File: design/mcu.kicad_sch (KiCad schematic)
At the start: 35 parts, among them J2 SWD_01X04, J3 DEBUG_SPI, U6 STM32H750VBTx, X1 ASTX-H11-25.000MHZ-T, X2 SIT8209AI-21-33S-100.000000X

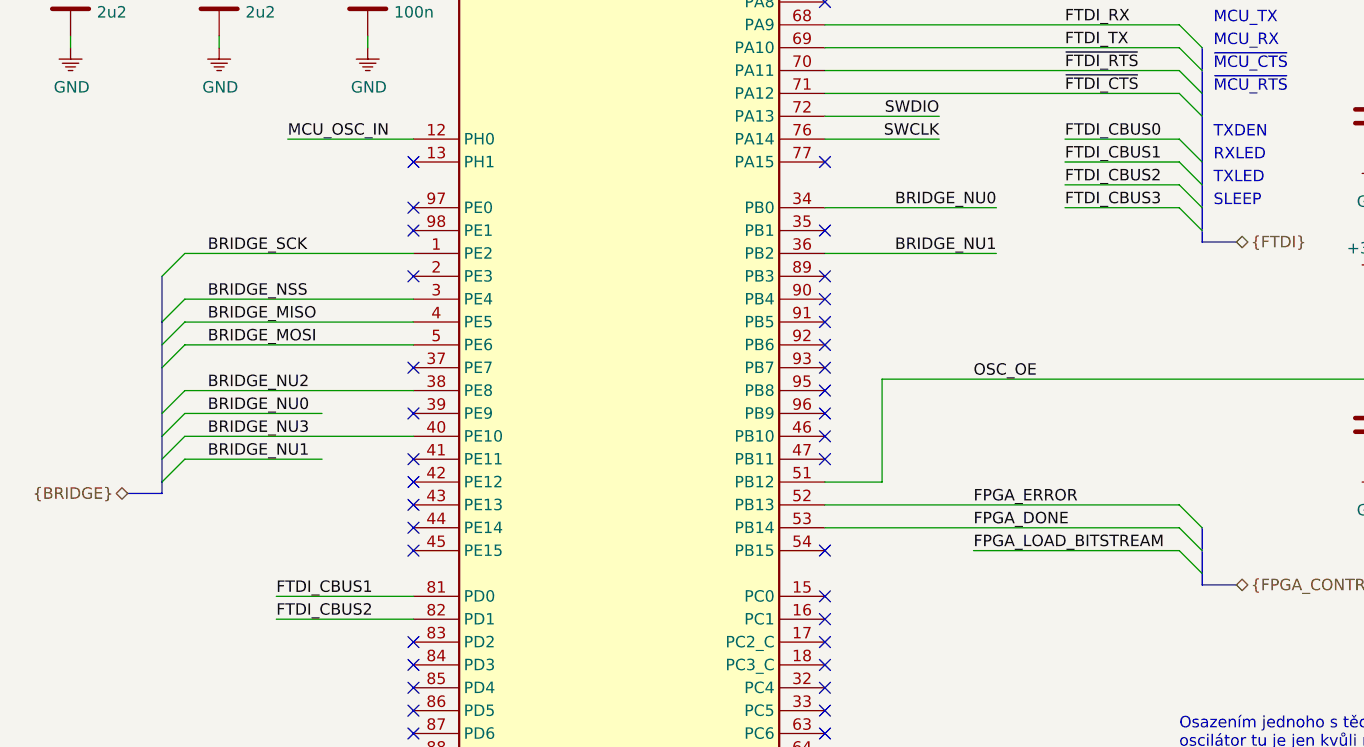
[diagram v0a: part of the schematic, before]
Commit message: Named button reset net
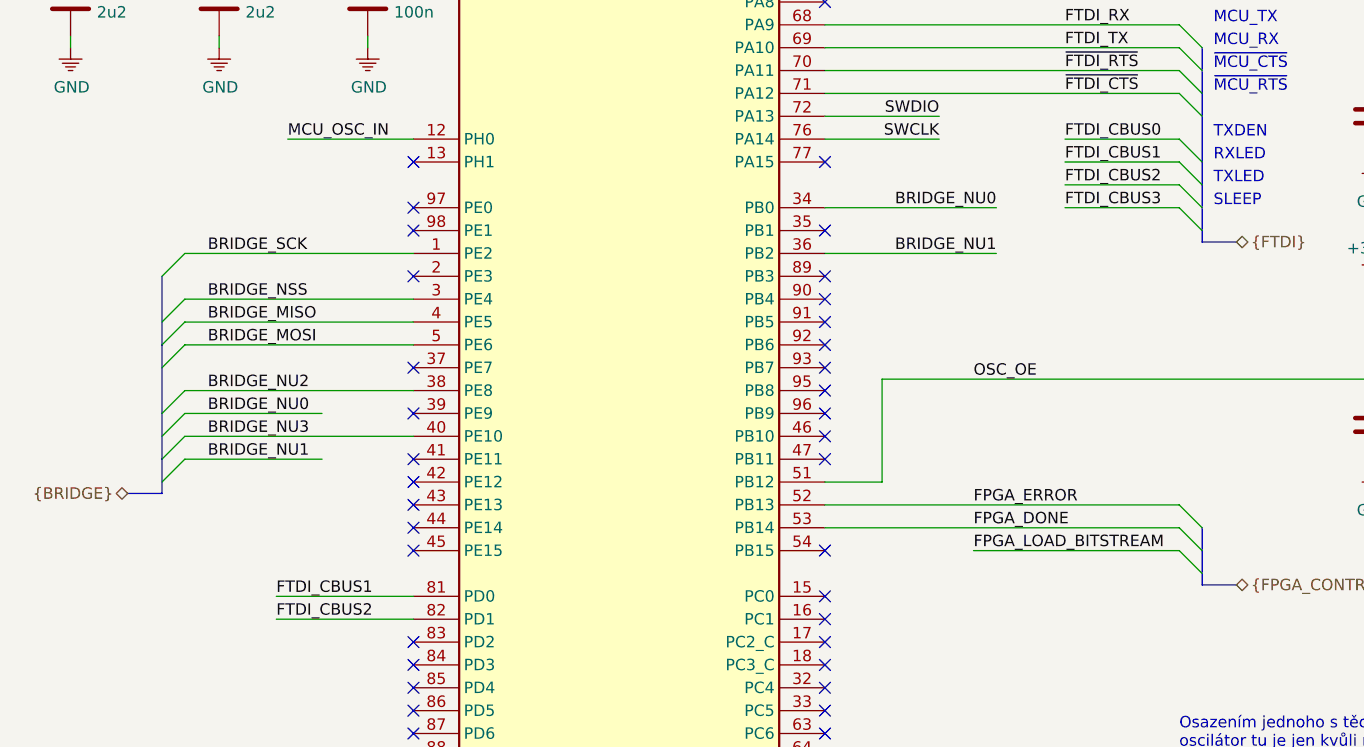
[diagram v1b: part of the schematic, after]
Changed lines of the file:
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@@
   (junction (at 236.22 25.4))
   (junction (at 262.89 26.67))
-  (no_connect (at 140.97 91.44))
+  (no_connect (at 140.97 45.72))
+  (no_connect (at 140.97 129.54))
+  (no_connect (at 95.25 109.22))
+  (no_connect (at 140.97 93.98))
+  (no_connect (at 95.25 132.08))
+  (no_connect (at 95.25 104.14))
   (no_connect (at 140.97 48.26))
-  (no_connect (at 95.25 99.06))
-  (no_connect (at 95.25 144.78))
-  (no_connect (at 140.97 43.18))
-  (no_connect (at 95.25 152.4))
-  (no_connect (at 140.97 83.82))
-  (no_connect (at 95.25 132.08))
-  (no_connect (at 140.97 40.64))
-  (no_connect (at 95.25 114.3))
-  (no_connect (at 95.25 116.84))
-  (no_connect (at 140.97 76.2))
-  (no_connect (at 140.97 129.54))
-  (no_connect (at 95.25 88.9))
-  (no_connect (at 140.97 45.72))
-  (no_connect (at 95.25 137.16))
-  (no_connect (at 140.97 96.52))
-  (no_connect (at 95.25 129.54))
-  (no_connect (at 95.25 149.86))
-  (no_connect (at 95.25 142.24))
-  (no_connect (at 140.97 134.62))
-  (no_connect (at 140.97 58.42))
-  (no_connect (at 95.25 76.2))
-  (no_connect (at 95.25 134.62))
-  (no_connect (at 140.97 144.78))
-  (no_connect (at 95.25 81.28))
+  (no_connect (at 140.97 53.34))
+  (no_connect (at 140.97 142.24))
+  (no_connect (at 95.25 139.7))
+  (no_connect (at 140.97 139.7))
+  (no_connect (at 140.97 157.48))
+  (no_connect (at 140.97 106.68))
   (no_connect (at 140.97 127))
-  (no_connect (at 95.25 139.7))
-  (no_connect (at 140.97 104.14))
-  (no_connect (at 140.97 162.56))
-  (no_connect (at 140.97 124.46))
-  (no_connect (at 95.25 83.82))
-  (no_connect (at 140.97 109.22))
+  (no_connect (at 140.97 137.16))
   (no_connect (at 140.97 38.1))
   (no_connect (at 140.97 99.06))
-  (no_connect (at 140.97 93.98))
-  (no_connect (at 140.97 137.16))
-  (no_connect (at 140.97 106.68))
-  (no_connect (at 140.97 142.24))
+  (no_connect (at 95.25 83.82))
+  (no_connect (at 95.25 88.9))
+  (no_connect (at 140.97 55.88))
+  (no_connect (at 95.25 81.28))
   (no_connect (at 140.97 50.8))
-  (no_connect (at 95.25 104.14))
+  (no_connect (at 95.25 134.62))
+  (no_connect (at 140.97 91.44))
+  (no_connect (at 140.97 96.52))
+  (no_connect (at 140.97 162.56))
+  (no_connect (at 95.25 76.2))
+  (no_connect (at 95.25 137.16))
+  (no_connect (at 95.25 129.54))
+  (no_connect (at 140.97 43.18))
+  (no_connect (at 95.25 149.86))
+  (no_connect (at 95.25 111.76))
+  (no_connect (at 140.97 76.2))
   (no_connect (at 140.97 149.86))
   (no_connect (at 140.97 119.38))
+  (no_connect (at 140.97 134.62))
+  (no_connect (at 140.97 88.9))
+  (no_connect (at 140.97 104.14))
+  (no_connect (at 95.25 144.78))
+  (no_connect (at 140.97 144.78))
+  (no_connect (at 95.25 152.4))
+  (no_connect (at 140.97 132.08))
+  (no_connect (at 140.97 109.22))
+  (no_connect (at 140.97 101.6))
+  (no_connect (at 140.97 58.42))
+  (no_connect (at 95.25 142.24))
+  (no_connect (at 95.25 114.3))
+  (no_connect (at 95.25 147.32))
+  (no_connect (at 140.97 83.82))
+  (no_connect (at 95.25 99.06))
+  (no_connect (at 95.25 116.84))
   (no_connect (at 95.25 119.38))
-  (no_connect (at 140.97 157.48))
-  (no_connect (at 140.97 88.9))
-  (no_connect (at 95.25 147.32))
-  (no_connect (at 140.97 139.7))
-  (no_connect (at 140.97 55.88))
-  (no_connect (at 140.97 101.6))
-  (no_connect (at 95.25 111.76))
-  (no_connect (at 95.25 109.22))
-  (no_connect (at 140.97 132.08))
-  (no_connect (at 140.97 53.34))
+  (no_connect (at 140.97 124.46))
+  (no_connect (at 140.97 40.64))
   (bus_entry (at 67.31 88.9) (size 2.54 -2.54))
   (bus_entry (at 67.31 93.98) (size 2.54 -2.54))
@@
   (wire (pts (xy 274.32 100.33) (xy 274.32 147.32)))
   (bus (pts (xy 63.5 113.03) (xy 67.31 113.03)))
-  (bus (pts (xy 67.31 88.9) (xy 67.31 93.98)))
-  (bus (pts (xy 67.31 93.98) (xy 67.31 99.06)))
-  (bus (pts (xy 67.31 99.06) (xy 67.31 106.68)))
-  (bus (pts (xy 67.31 106.68) (xy 67.31 111.76)))
-  (bus (pts (xy 67.31 111.76) (xy 67.31 113.03)))
+  (bus (pts (xy 67.31 88.9) (xy 67.31 96.52)))
+  (bus (pts (xy 67.31 96.52) (xy 67.31 104.14)))
+  (bus (pts (xy 67.31 104.14) (xy 67.31 109.22)))
+  (bus (pts (xy 67.31 109.22) (xy 67.31 113.03)))
   (bus (pts (xy 182.88 63.5) (xy 182.88 68.58)))
   (bus (pts (xy 182.88 68.58) (xy 182.88 76.2)))
-  (bus (pts (xy 182.88 76.2) (xy 182.88 81.28)))
-  (bus (pts (xy 182.88 81.28) (xy 182.88 85.09)))
+  (bus (pts (xy 182.88 76.2) (xy 182.88 78.74)))
+  (bus (pts (xy 182.88 78.74) (xy 182.88 83.82)))
+  (bus (pts (xy 182.88 83.82) (xy 182.88 85.09)))
   (bus (pts (xy 182.88 85.09) (xy 186.69 85.09)))
-  (bus (pts (xy 182.88 116.84) (xy 182.88 121.92)))
-  (bus (pts (xy 182.88 121.92) (xy 182.88 123.19)))
+  (bus (pts (xy 182.88 116.84) (xy 182.88 119.38)))
+  (bus (pts (xy 182.88 119.38) (xy 182.88 123.19)))
   (bus (pts (xy 186.69 123.19) (xy 182.88 123.19)))
   (polyline (pts (xy 186.69 13.97) (xy 186.69 44.45)))

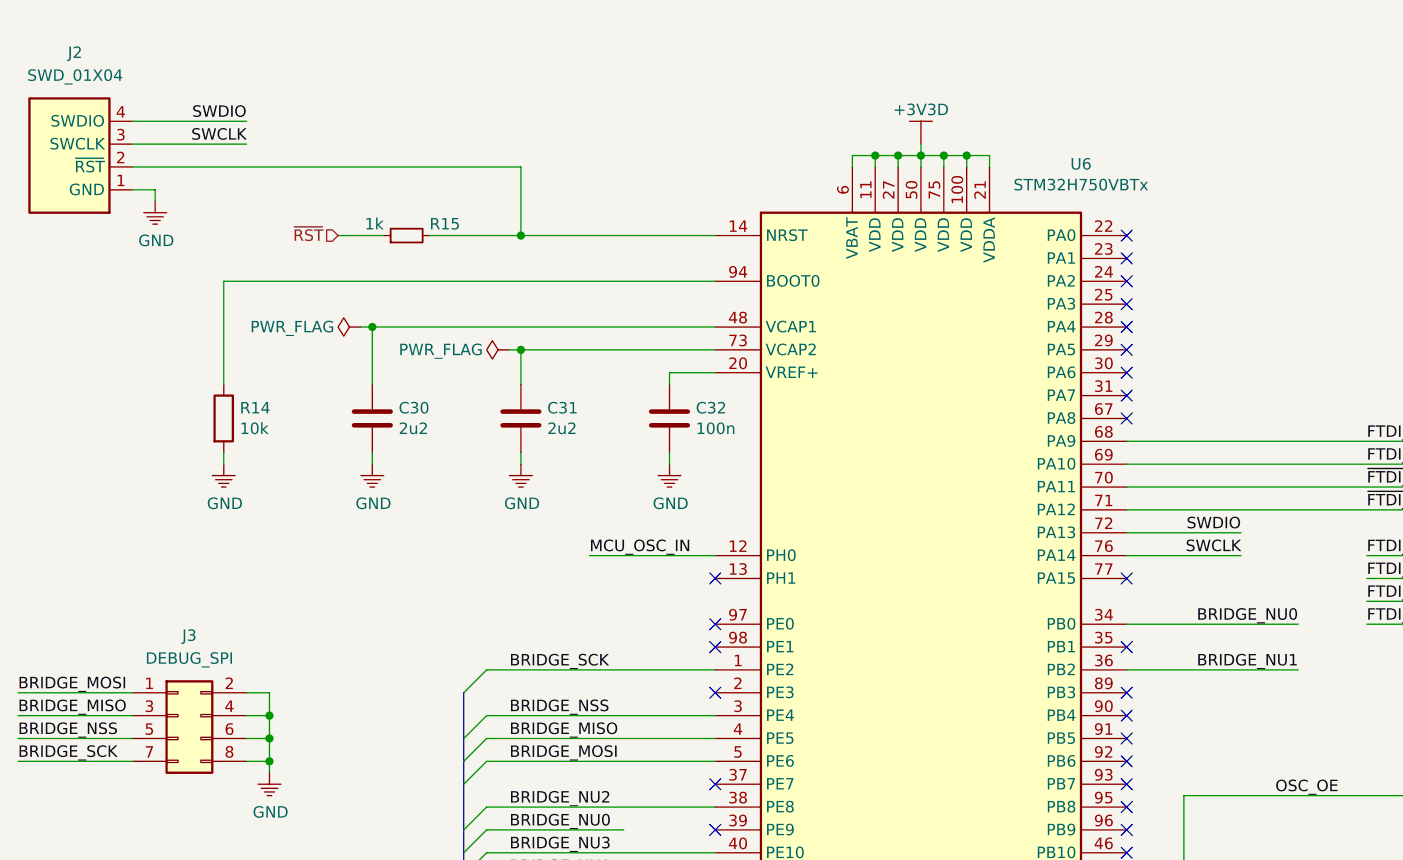
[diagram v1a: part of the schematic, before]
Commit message: Chenged SWD connector from 4 pins to 6 pins
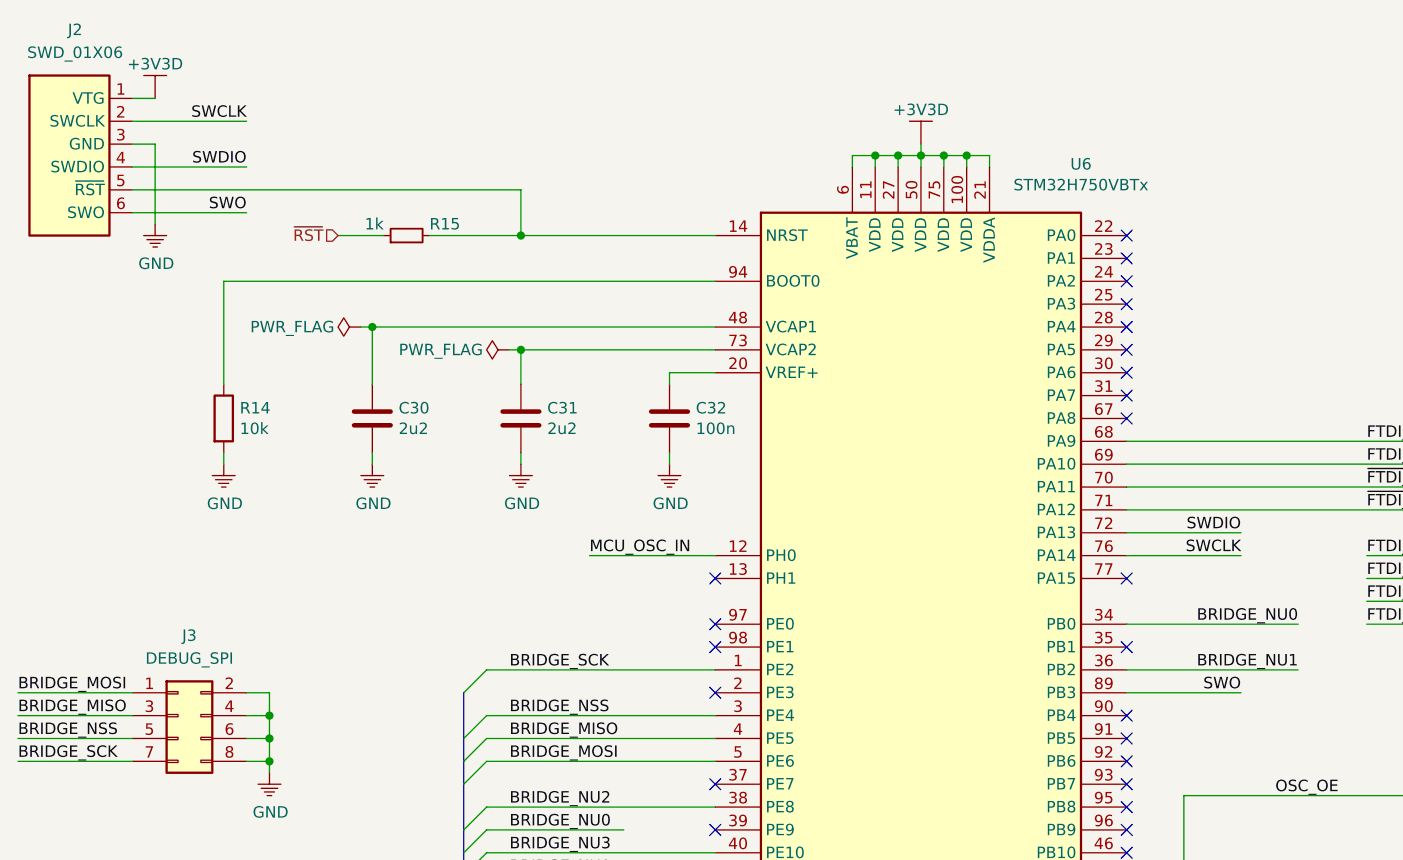
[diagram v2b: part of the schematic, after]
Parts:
- removed J2: SWD_01X04, Connector_PinHeader_2.54mm:PinHeader_1x04_P2.54mm_Vertical, symbol KLIB_Connector_Prog:SWD_01X04
- added J2: SWD_01X06, Connector_PinHeader_2.54mm:PinHeader_1x06_P2.54mm_Vertical, symbol KLIB_Connector_Prog:SWD_01X06
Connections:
- net +3V3D: now also J2.1 (VTG)
- net GND: now also J2.3 (GND)
- net SWCLK: now also J2.2 (SWCLK)
- net SWDIO: now also J2.4 (SWDIO)
- net at R15.2, U6.14 (NRST): now also J2.5 (~RST)
- net SWO: now reaches U6.89 (PB3)
- net SWO: now also J2.6 (SWO)
- no-connect marks 54 -> 53
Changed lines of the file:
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@@
   (no_connect (at 140.97 119.38))
   (no_connect (at 140.97 134.62))
-  (no_connect (at 140.97 88.9))
   (no_connect (at 140.97 104.14))
   (no_connect (at 95.25 144.78))
@@
   (wire (pts (xy 24.13 154.94) (xy 24.13 163.83)))
   (wire (pts (xy 24.13 171.45) (xy 24.13 172.72)))
+  (wire (pts (xy 30.48 22.86) (xy 33.02 22.86)))
   (wire (pts (xy 30.48 25.4) (xy 43.18 25.4)))
-  (wire (pts (xy 30.48 27.94) (xy 43.18 27.94)))
-  (wire (pts (xy 30.48 30.48) (xy 73.66 30.48)))
-  (wire (pts (xy 30.48 33.02) (xy 33.02 33.02)))
-  (wire (pts (xy 33.02 33.02) (xy 33.02 34.29)))
+  (wire (pts (xy 30.48 30.48) (xy 43.18 30.48)))
+  (wire (pts (xy 30.48 33.02) (xy 73.66 33.02)))
+  (wire (pts (xy 30.48 35.56) (xy 43.18 35.56)))
+  (wire (pts (xy 33.02 27.94) (xy 30.48 27.94)))
+  (wire (pts (xy 33.02 36.83) (xy 33.02 27.94)))
   (wire (pts (xy 35.56 157.48) (xy 35.56 163.83)))
   (wire (pts (xy 35.56 171.45) (xy 35.56 172.72)))
@@
   (wire (pts (xy 69.85 109.22) (xy 85.09 109.22)))
   (wire (pts (xy 72.39 50.8) (xy 73.66 50.8)))
-  (wire (pts (xy 73.66 30.48) (xy 73.66 38.1)))
+  (wire (pts (xy 73.66 33.02) (xy 73.66 38.1)))
   (wire (pts (xy 73.66 38.1) (xy 95.25 38.1)))
   (wire (pts (xy 73.66 50.8) (xy 73.66 54.61)))
@@
   (wire (pts (xy 140.97 81.28) (xy 160.02 81.28)))
   (wire (pts (xy 140.97 86.36) (xy 160.02 86.36)))
+  (wire (pts (xy 140.97 88.9) (xy 153.67 88.9)))
   (wire (pts (xy 140.97 114.3) (xy 180.34 114.3)))
   (wire (pts (xy 140.97 116.84) (xy 180.34 116.84)))
@@
     (effects (font (size 1.27 1.27)) (justify left bottom))
   )
-  (label "SWDIO" (at 43.18 25.4 180)
+  (label "SWCLK" (at 43.18 25.4 180)
     (effects (font (size 1.27 1.27)) (justify right bottom))
   )
-  (label "SWCLK" (at 43.18 27.94 180)
+  (label "SWDIO" (at 43.18 30.48 180)
+    (effects (font (size 1.27 1.27)) (justify right bottom))
+  )
+  (label "SWO" (at 43.18 35.56 180)
     (effects (font (size 1.27 1.27)) (justify right bottom))
   )
@@
     (effects (font (size 1.27 1.27)) (justify right bottom))
   )
+  (label "SWO" (at 153.67 88.9 180)
+    (effects (font (size 1.27 1.27)) (justify right bottom))
+  )
   (label "FTDI_CBUS3" (at 156.21 152.4 180)
     (effects (font (size 1.27 1.27)) (justify right bottom))
@@
     )
   )
-  (symbol (lib_id "KLIB_Power:GND") (at 33.02 34.29 0) (unit 1)
-    (property "Reference" "#PWR059" (id 0) (at 33.02 39.37 0)
-      (effects (font (size 1.27 1.27)) hide)
-    )
-    (property "Value" "GND" (id 1) (at 33.147 38.6842 0))
-    (property "Footprint" "" (id 2) (at 33.02 34.29 0)
-      (effects (font (size 1.27 1.27)) hide)
-    )
-    (property "Datasheet" "" (id 3) (at 33.02 34.29 0)
+  (symbol (lib_id "KLIB_Power:+3V3D") (at 33.02 22.86 0) (unit 1)
+    (property "Reference" "#PWR0219" (id 0) (at 33.02 30.48 0)
+      (effects (font (size 1.27 1.27)) hide)
+    )
+    (property "Value" "+3V3D" (id 1) (at 33.02 19.05 0))
+    (property "Footprint" "" (id 2) (at 33.02 22.86 0)
+      (effects (font (size 1.27 1.27)) hide)
+    )
+    (property "Datasheet" "" (id 3) (at 33.02 22.86 0)
+      (effects (font (size 1.27 1.27)) hide)
+    )
+  )
+  (symbol (lib_id "KLIB_Power:GND") (at 33.02 36.83 0) (unit 1)
+    (property "Reference" "#PWR059" (id 0) (at 33.02 41.91 0)
+      (effects (font (size 1.27 1.27)) hide)
+    )
+    (property "Value" "GND" (id 1) (at 33.147 41.2242 0))
+    (property "Footprint" "" (id 2) (at 33.02 36.83 0)
+      (effects (font (size 1.27 1.27)) hide)
+    )
+    (property "Datasheet" "" (id 3) (at 33.02 36.83 0)
       (effects (font (size 1.27 1.27)) hide)
     )
@@
     )
   )
-  (symbol (lib_id "KLIB_Connector_Prog:SWD_01X04") (at 25.4 30.48 0) (unit 1)
-    (property "Reference" "J2" (id 0) (at 24.13 17.78 0))
-    (property "Value" "SWD_01X04" (id 1) (at 24.13 20.32 0))
-    (property "Footprint" "Connector_PinHeader_2.54mm:PinHeader_1x04_P2.54mm_Vertical" (id 2) (at 24.13 40.64 0)
-      (effects (font (size 1.27 1.27)) hide)
-    )
-    (property "Datasheet" "~" (id 3) (at 35.56 20.32 0)
-      (effects (font (size 1.27 1.27)) hide)
-    )
+  (symbol (lib_id "KLIB_Connector_Prog:SWD_01X06") (at 25.4 27.94 0) (unit 1)
+    (property "Reference" "J2" (id 0) (at 24.13 15.24 0))
+    (property "Value" "SWD_01X06" (id 1) (at 24.13 17.78 0))
+    (property "Footprint" "Connector_PinHeader_2.54mm:PinHeader_1x06_P2.54mm_Vertical" (id 2) (at 24.13 43.18 0)
+      (effects (font (size 1.27 1.27)) hide)
+    )
+    (property "Datasheet" "~" (id 3) (at 35.56 17.78 0)
+      (effects (font (size 1.27 1.27)) hide)
+    )
